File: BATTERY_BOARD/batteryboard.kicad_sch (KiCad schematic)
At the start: 67 parts, among them IC1 R5460N233AF-TR-FE, J1 1042, J10 SM02B-SFHRS-TF_LF__SN_, J11 F3311A7H121014E200, J13 SM02B-SFHRS-TF_LF__SN_, J14 SM02B-SFHRS-TF_LF__SN_, J15 SM02B-SFHRS-TF_LF__SN_, J16 SM02B-SFHRS-TF_LF__SN_, J2 1042, J3 1042, J4 1042, J5 1042, J6 1042, J7 SM02B-SFHRS-TF_LF__SN_, J8 SM02B-SFHRS-TF_LF__SN_, J9 SM02B-SFHRS-TF_LF__SN_, K1 9-1462038-9, Q1 IRF7458, Q2 IRF7458, Q20 NDS8434, Q21 NDS8434, Q4 IRLML2803, Q5 IRLML2803, Q6 MMBT2222AT

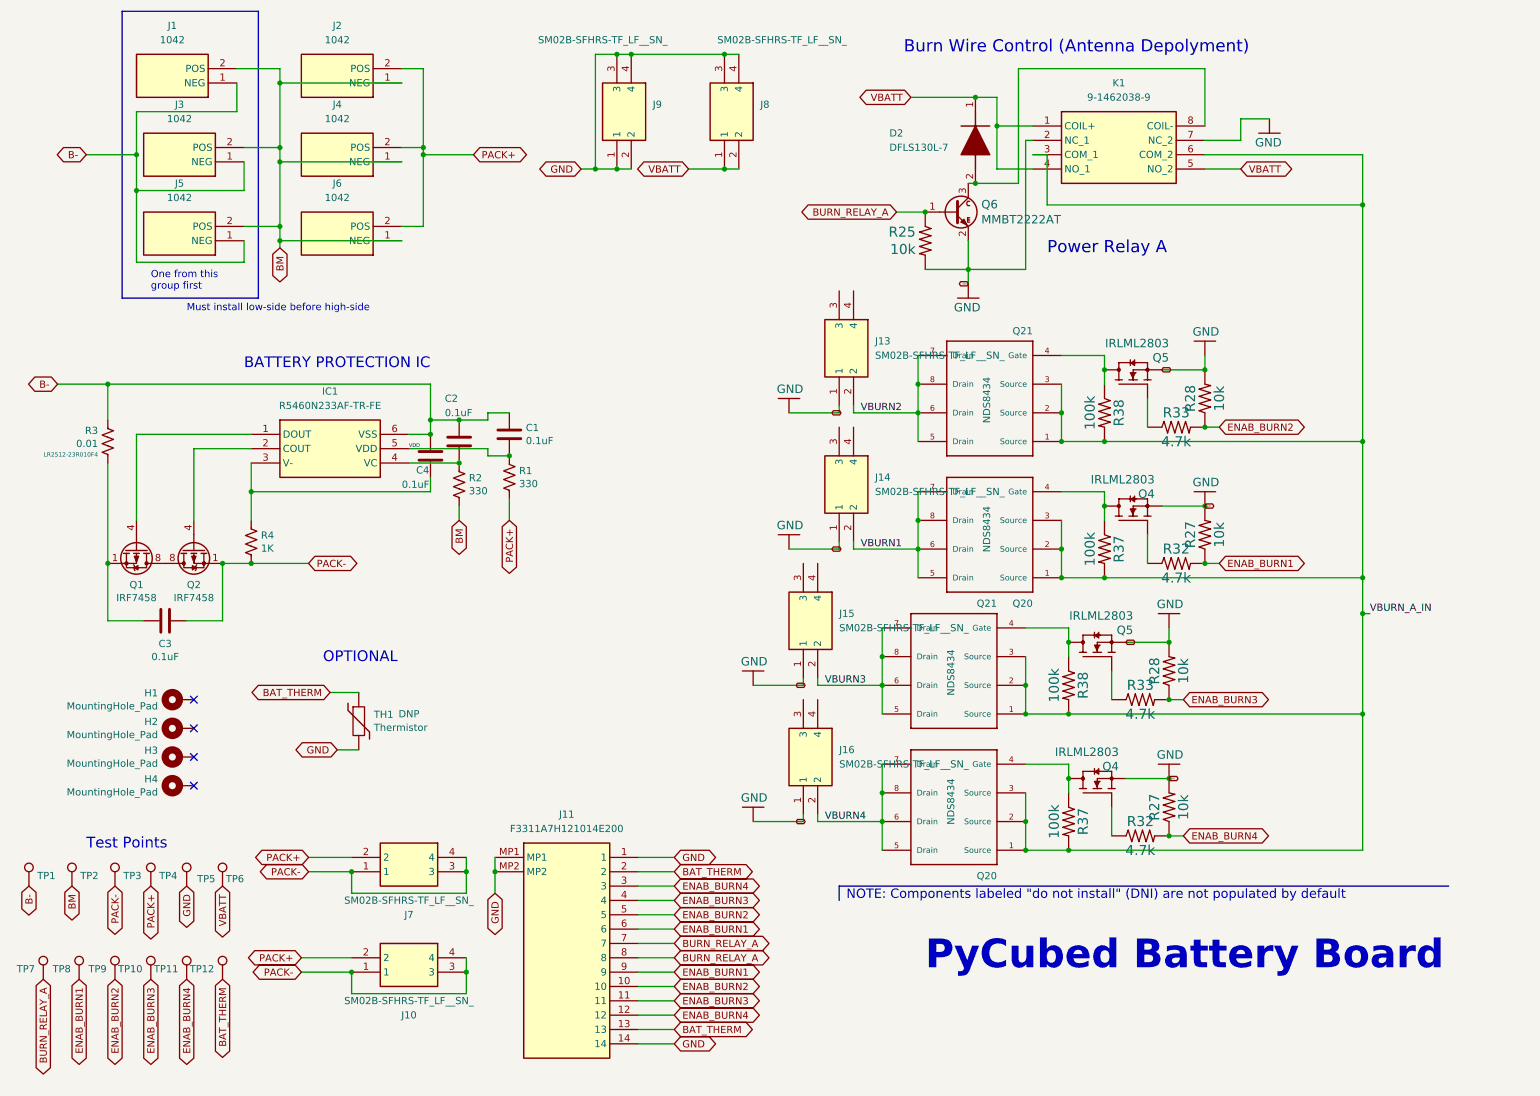
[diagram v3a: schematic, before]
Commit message: Battery Board all changes done
Based on feedback by Neil
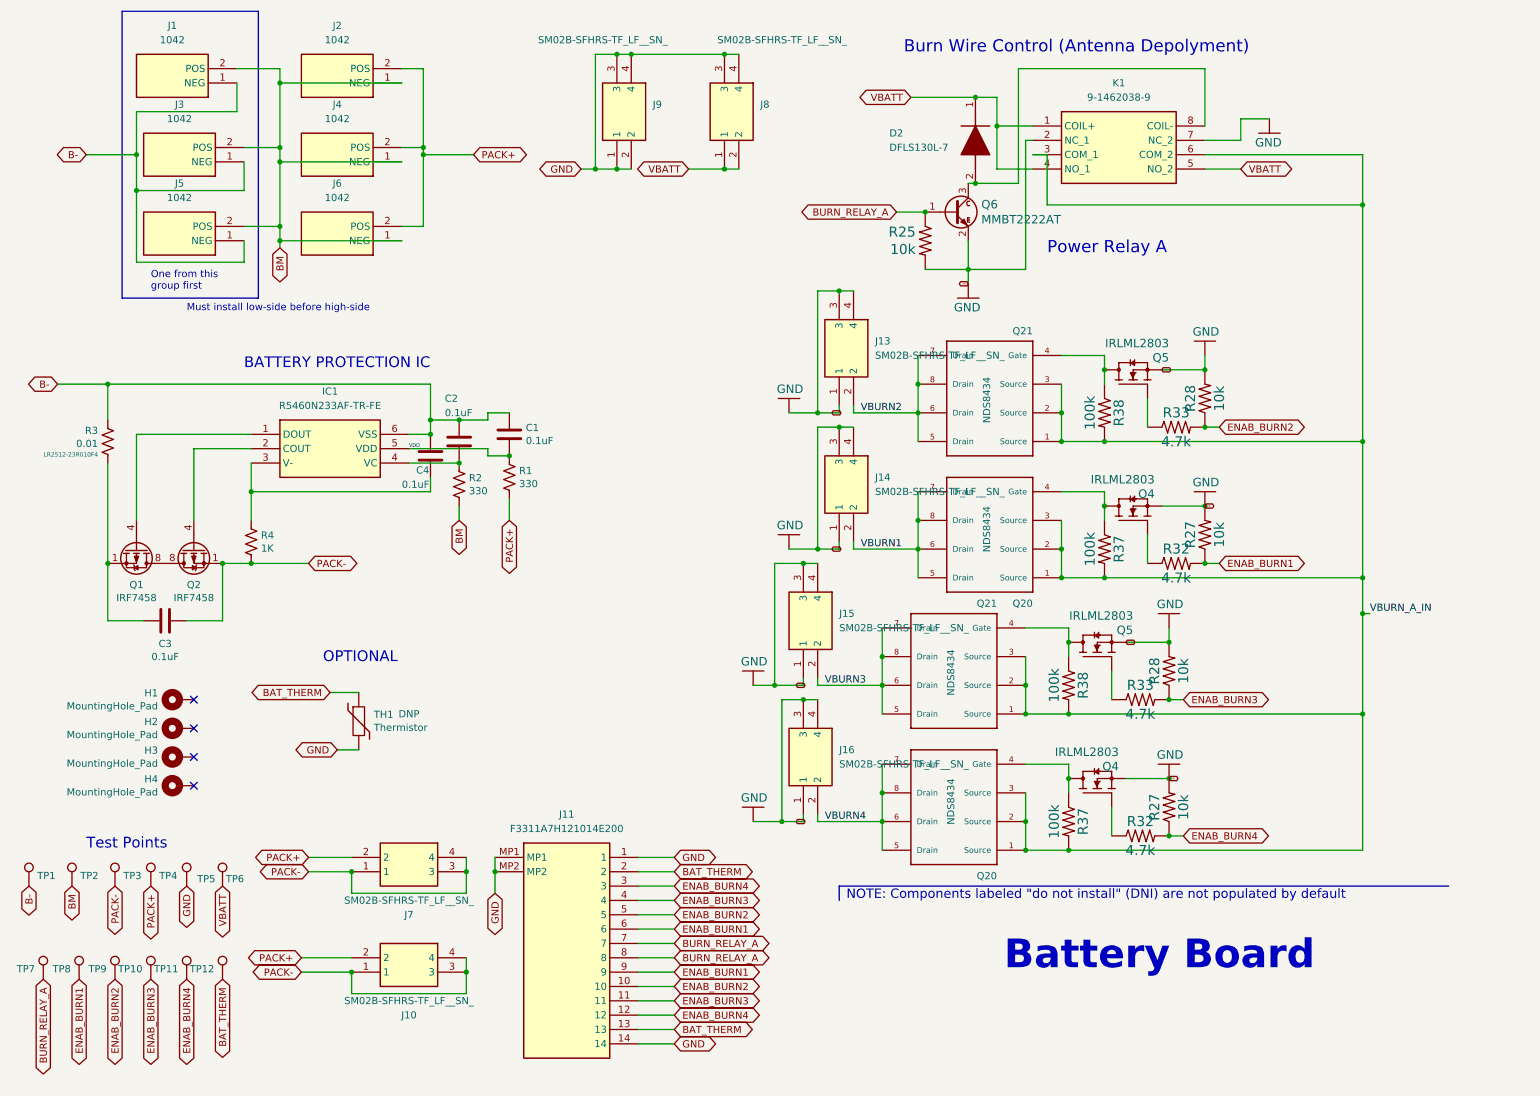
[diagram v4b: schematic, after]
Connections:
- net GND: now also J13.3, J13.4, J14.3, J14.4, J15.3, J15.4, J16.3, J16.4
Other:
- note added: "Battery Board"
- note removed: "PyCubed Battery Board"
- company: Max Holliday -> CMU
- title: PyCubed Battery Board -> Battery Board
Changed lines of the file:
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@@
   (paper "USLetter")
   (title_block
-    (title "PyCubed Battery Board")
-    (date "2021-03-07")
-    (rev "v01b")
-    (company "Max Holliday")
+    (title "Battery Board")
+    (date "2024-01-29")
+    (rev "1.0")
+    (company "CMU")
   )
   (junction (at 172.72 109.22) (diameter 0) (color 0 0 0 0)
@@
   (junction (at 186.69 34.29) (diameter 0) (color 0 0 0 0)
   )
+  (junction (at 147.32 133.35) (diameter 0) (color 0 0 0 0)
+  )
   (junction (at 97.79 166.37) (diameter 0) (color 0 0 0 0)
   )
@@
   (junction (at 121.92 21.59) (diameter 0) (color 0 0 0 0)
   )
+  (junction (at 158.75 87.63) (diameter 0) (color 0 0 0 0)
+  )
   (junction (at 191.77 138.43) (diameter 0) (color 0 0 0 0)
   )
@@
   (junction (at 251.46 114.3) (diameter 0) (color 0 0 0 0)
   )
+  (junction (at 152.4 135.89) (diameter 0) (color 0 0 0 0)
+  )
   (junction (at 166.37 157.48) (diameter 0) (color 0 0 0 0)
   )
@@
   (junction (at 91.44 93.98) (diameter 0) (color 0 0 0 0)
   )
+  (junction (at 152.4 111.76) (diameter 0) (color 0 0 0 0)
+  )
   (junction (at 172.72 104.14) (diameter 0) (color 0 0 0 0)
   )
@@
   (junction (at 199.39 125.73) (diameter 0) (color 0 0 0 0)
   )
+  (junction (at 154.94 109.22) (diameter 0) (color 0 0 0 0)
+  )
+  (junction (at 154.94 85.09) (diameter 0) (color 0 0 0 0)
+  )
   (junction (at 217.17 160.02) (diameter 0) (color 0 0 0 0)
   )
@@
   (junction (at 191.77 162.56) (diameter 0) (color 0 0 0 0)
   )
+  (junction (at 158.75 63.5) (diameter 0) (color 0 0 0 0)
+  )
   (junction (at 59.69 26.67) (diameter 0) (color 0 0 0 0)
   )
@@
   )
   (junction (at 166.37 128.27) (diameter 0) (color 0 0 0 0)
+  )
+  (junction (at 148.59 157.48) (diameter 0) (color 0 0 0 0)
   )
   (junction (at 86.36 88.9) (diameter 0) (color 0 0 0 0)
@@
     (stroke (width 0) (type default))
   )
+  (wire (pts (xy 154.94 109.22) (xy 158.75 109.22))
+    (stroke (width 0) (type default))
+  )
   (wire (pts (xy 53.34 38.1) (xy 59.69 38.1))
     (stroke (width 0) (type default))
@@
     (stroke (width 0) (type default))
   )
+  (wire (pts (xy 152.4 111.76) (xy 154.94 111.76))
+    (stroke (width 0) (type default))
+  )
   (wire (pts (xy 81.28 24.13) (xy 85.09 24.13))
     (stroke (width 0) (type default))
@@
     (stroke (width 0) (type default))
   )
+  (wire (pts (xy 158.75 87.63) (xy 161.29 87.63))
+    (stroke (width 0) (type default))
+  )
   (wire (pts (xy 85.09 39.37) (xy 85.09 52.07))
     (stroke (width 0) (type default))
@@
     (stroke (width 0) (type default))
   )
-  (wire (pts (xy 143.51 133.35) (xy 152.4 133.35))
+  (wire (pts (xy 143.51 133.35) (xy 147.32 133.35))
     (stroke (width 0) (type default))
   )
@@
     (stroke (width 0) (type default))
   )
-  (wire (pts (xy 149.86 109.22) (xy 158.75 109.22))
+  (wire (pts (xy 149.86 109.22) (xy 154.94 109.22))
     (stroke (width 0) (type default))
   )
@@
     (stroke (width 0) (type default))
   )
-  (wire (pts (xy 143.51 157.48) (xy 152.4 157.48))
+  (wire (pts (xy 143.51 157.48) (xy 148.59 157.48))
     (stroke (width 0) (type default))
   )
@@
     (stroke (width 0) (type default))
   )
+  (wire (pts (xy 158.75 87.63) (xy 154.94 87.63))
+    (stroke (width 0) (type default))
+  )
   (wire (pts (xy 43.18 121.92) (xy 49.53 121.92))
     (stroke (width 0) (type default))
@@
     (stroke (width 0) (type default))
   )
+  (wire (pts (xy 158.75 63.5) (xy 161.29 63.5))
+    (stroke (width 0) (type default))
+  )
   (wire (pts (xy 251.46 39.37) (xy 251.46 48.26))
     (stroke (width 0) (type default))
@@
     (stroke (width 0) (type default))
   )
-  (wire (pts (xy 149.86 85.09) (xy 158.75 85.09))
+  (wire (pts (xy 154.94 85.09) (xy 154.94 63.5))
+    (stroke (width 0) (type default))
+  )
+  (wire (pts (xy 149.86 85.09) (xy 154.94 85.09))
     (stroke (width 0) (type default))
   )
@@
     (stroke (width 0) (type default))
   )
+  (wire (pts (xy 152.4 135.89) (xy 148.59 135.89))
+    (stroke (width 0) (type default))
+  )
   (wire (pts (xy 213.36 106.68) (xy 213.36 111.76))
     (stroke (width 0) (type default))
@@
     (stroke (width 0) (type default))
   )
+  (wire (pts (xy 152.4 135.89) (xy 154.94 135.89))
+    (stroke (width 0) (type default))
+  )
+  (wire (pts (xy 154.94 87.63) (xy 154.94 109.22))
+    (stroke (width 0) (type default))
+  )
   (wire (pts (xy 85.09 38.1) (xy 85.09 39.37))
     (stroke (width 0) (type default))
@@
     (stroke (width 0) (type default))
   )
+  (wire (pts (xy 148.59 135.89) (xy 148.59 157.48))
+    (stroke (width 0) (type default))
+  )
   (wire (pts (xy 96.52 86.36) (xy 96.52 85.09))
     (stroke (width 0) (type default))
@@
     (stroke (width 0) (type default))
   )
+  (wire (pts (xy 148.59 157.48) (xy 152.4 157.48))
+    (stroke (width 0) (type default))
+  )
   (wire (pts (xy 85.09 39.37) (xy 93.98 39.37))
     (stroke (width 0) (type default))
@@
     (stroke (width 0) (type default))
   )
+  (wire (pts (xy 154.94 85.09) (xy 158.75 85.09))
+    (stroke (width 0) (type default))
+  )
+  (wire (pts (xy 147.32 111.76) (xy 147.32 133.35))
+    (stroke (width 0) (type default))
+  )
   (wire (pts (xy 198.12 74.93) (xy 205.74 74.93))
     (stroke (width 0) (type default))
@@
     (stroke (width 0) (type default))
   )
+  (wire (pts (xy 147.32 133.35) (xy 152.4 133.35))
+    (stroke (width 0) (type default))
+  )
   (wire (pts (xy 161.29 85.09) (xy 172.72 85.09))
     (stroke (width 0) (type default))
   )
+  (wire (pts (xy 152.4 111.76) (xy 147.32 111.76))
+    (stroke (width 0) (type default))
+  )
   (wire (pts (xy 138.43 21.59) (xy 140.97 21.59))
     (stroke (width 0) (type default))
@@
   )
   (wire (pts (xy 215.9 77.47) (xy 223.52 77.47))
+    (stroke (width 0) (type default))
+  )
+  (wire (pts (xy 154.94 63.5) (xy 158.75 63.5))
     (stroke (width 0) (type default))
   )
@@
     (effects (font (size 1.27 1.27)) (justify left bottom))
   )
-  (text "PyCubed Battery Board" (at 173.99 184.15 0)
+  (text "Battery Board" (at 187.96 184.15 0)
     (effects (font (size 5.08 5.08) (thickness 1.016) bold) (justify left bottom))
   )
